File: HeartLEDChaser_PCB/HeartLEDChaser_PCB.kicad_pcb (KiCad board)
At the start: 2 copper layers, 55.6 x 49.3 mm, 34 parts, among them U1 ICM7555CBAZ, U2 CD4017BM, U3 HT7733A, U4 HX SS12F44G4

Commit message: Routed PCB
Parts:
- H1: footprint MountingHole:MountingHole_2.7mm -> MountingHole:MountingHole_2.1mm
- moved C4 84.3 mm to (162.3, 90.4), turned to -90 degrees
- moved U3 83.7 mm to (160.3, 85.8), turned to 90 degrees
- moved S1 79.0 mm to (158.4, 90.4), turned to -90 degrees
- moved D10 77.3 mm to (154.2, 79.4)
- moved D6 77.3 mm to (143.9, 119.8)
- moved D7 77.3 mm to (158.7, 109.8)
- moved D8 77.3 mm to (168.3, 96.3)
- moved R12 77.3 mm to (157.5, 79.4)
- moved R7 77.3 mm to (134.6, 113.6)
- moved R8 77.3 mm to (145.2, 115.4)
- moved R9 77.3 mm to (155.6, 113.5)
- moved D2 77.3 mm to (135.8, 79.3)
- moved D3 77.3 mm to (122.8, 81.4)
- moved D4 77.3 mm to (121.8, 96.3)
- moved D5 77.3 mm to (131.5, 109.8)
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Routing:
- net Net-(D9-A): track 0.00 -> 52.9 mm, vias 0 -> 1
- net +3V3: track 0.00 -> 43.6 mm
- net Net-(D8-A): track 0.00 -> 35.1 mm, vias 0 -> 1
- net Net-(U1-THRESHOLD): track 0.00 -> 31.3 mm
- net Net-(D10-A): track 0.00 -> 30.8 mm, vias 0 -> 1
- net Net-(D3-A): track 0.00 -> 29.3 mm
- net Net-(D6-A): track 0.00 -> 27.5 mm, vias 0 -> 1
- net Net-(D7-A): track 0.00 -> 25.8 mm, vias 0 -> 1
- net Net-(D2-A): track 0.00 -> 24.1 mm, vias 0 -> 1
- net +3V0: track 0.00 -> 23.7 mm
- net ASTABLE_OUTPUT: track 0.00 -> 20.9 mm
- net Net-(D4-A): track 0.00 -> 19.7 mm
- net Net-(D1-A): track 0.00 -> 17.1 mm
- net Net-(D5-A): track 0.00 -> 15.4 mm
- net GND: track 0.00 -> 15.4 mm, vias 0 -> 2
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- added copper zone on B.Cu, net GND
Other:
- board size 55.6 x 49.3 mm -> 55.6 x 49.4 mm

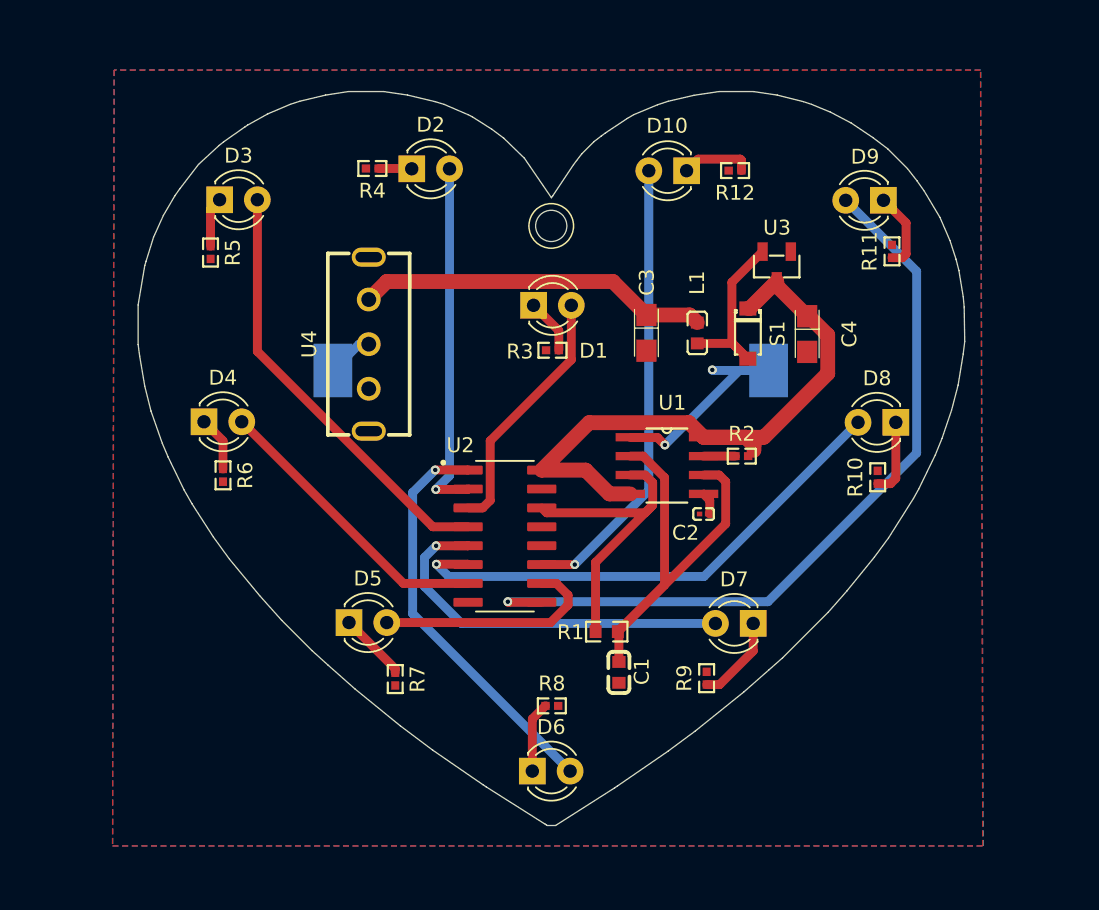
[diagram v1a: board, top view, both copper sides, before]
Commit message: Added logos
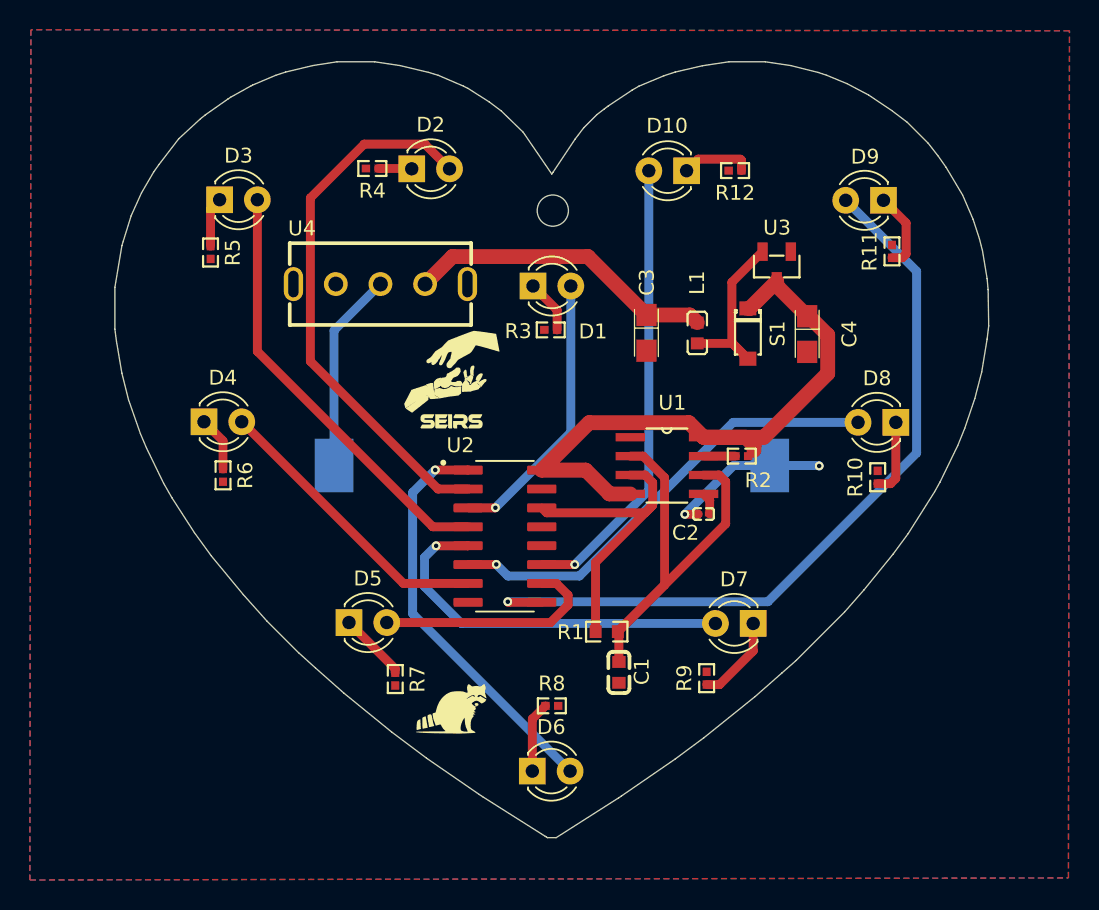
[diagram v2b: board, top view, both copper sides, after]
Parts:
- added G***: LOGO, FOOTPRINTS:seirslogo, F.Cu at (138.4, 93.4)
- added G***: LOGO, FOOTPRINTS:raccoonimage, F.Cu at (138.3, 115.6)
- moved BT1 6.39 mm to (145.2, 99.2)
- moved U4 4.12 mm to (133.7, 87.0), turned to 0 degrees
- moved R3 1.37 mm to (145.1, 90.1)
- moved D1 1.30 mm to (143.9, 87.2)
- moved H1 1.04 mm to (145.2, 82.1)
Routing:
- net Net-(D2-A): track 24.1 -> 36.7 mm, vias 1 -> 0
- net Net-(BT1-+): track 3.14 -> 13.5 mm
- net Net-(D8-A): track 35.1 -> 30.8 mm
- net GND: track 15.4 -> 11.3 mm
- net +3V0: track 23.7 -> 20.9 mm
- net Net-(D1-A): track 17.1 -> 18.8 mm, vias 0 -> 1
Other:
- board size 55.6 x 49.4 mm -> 58.8 x 52.2 mm
- board text added: "Happy Valentine's Day ( ˘ ³˘)♥"
- board text added: "https://github.com/fectec/HeartLEDChaser"

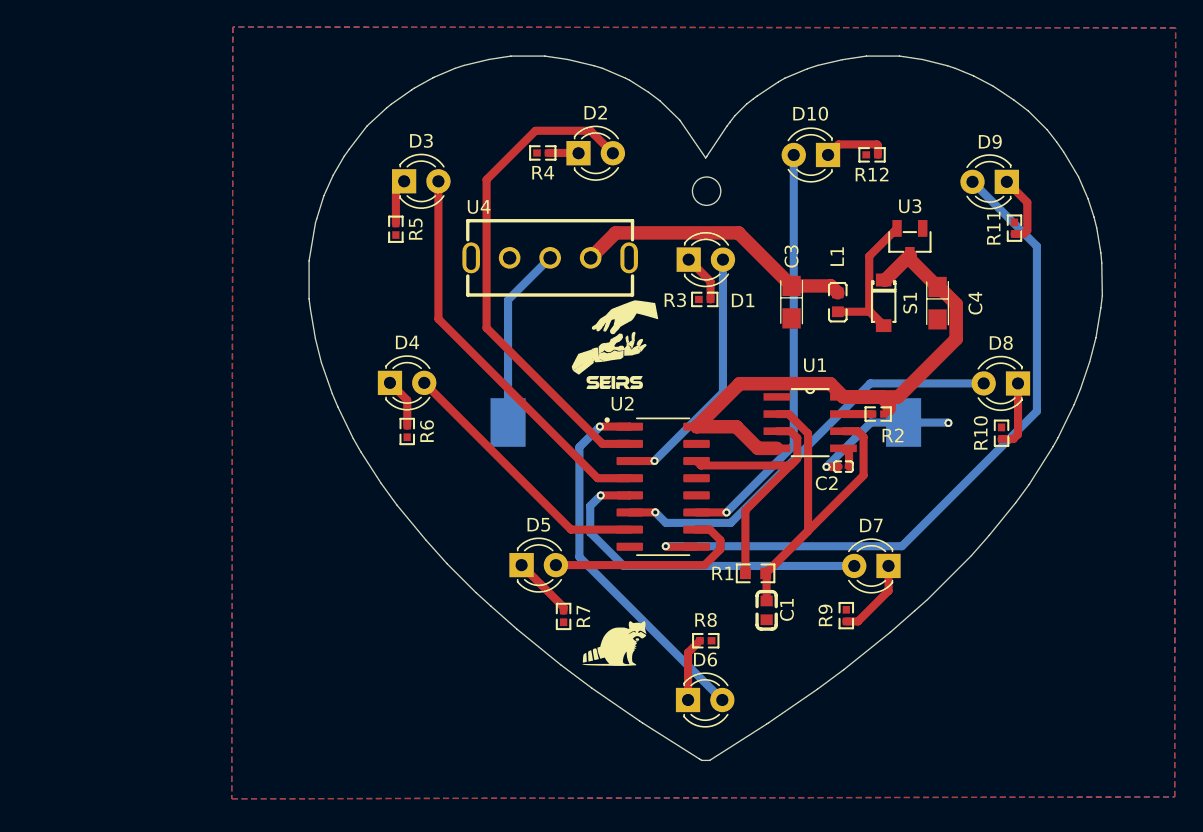
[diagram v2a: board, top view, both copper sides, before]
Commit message: Improved layout & routing
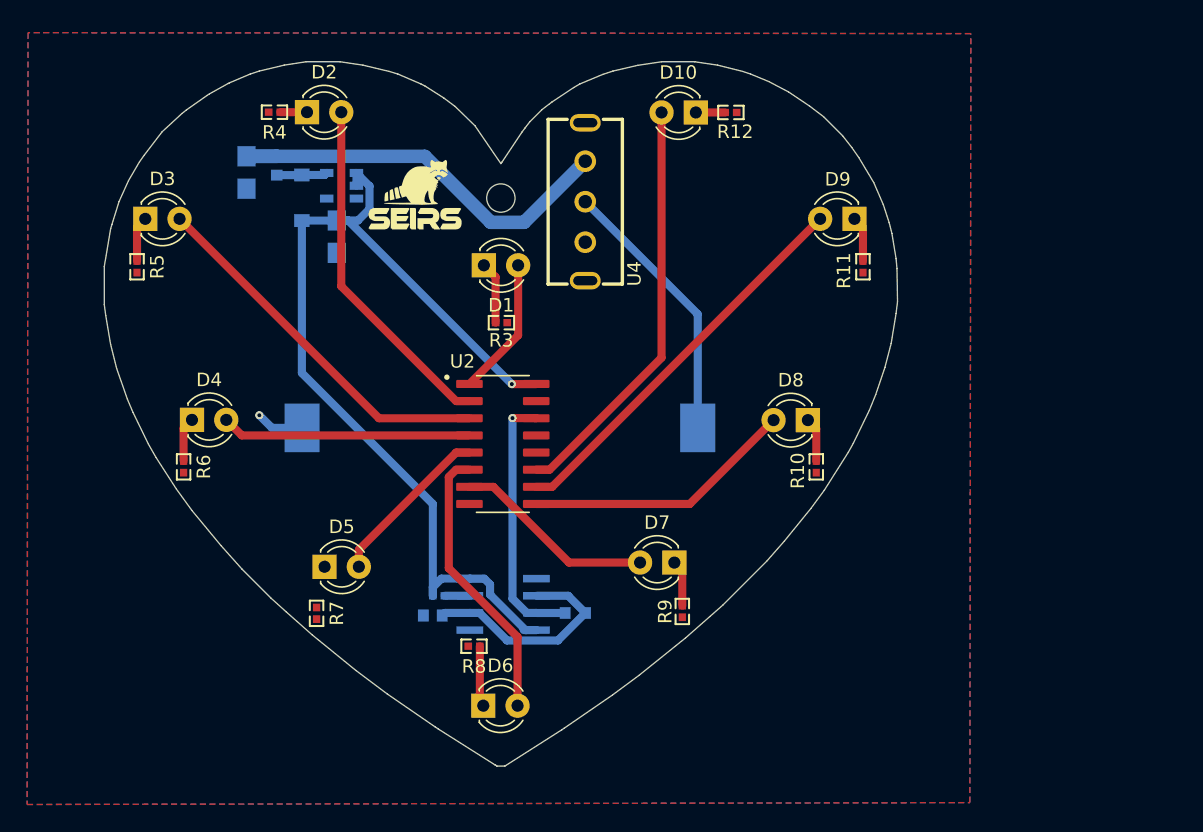
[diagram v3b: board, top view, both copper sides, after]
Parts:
- removed C2: 47nF, FOOTPRINTS:C85925
- C1, C3, C4, L1, R1, R2, S1, U1: moved to B.Cu
- U3: value HT7733A -> HT7750A; footprint FOOTPRINTS:HT7733A -> FOOTPRINTS:HT7750A; moved to B.Cu
- moved C4 44.8 mm to (117.8, 85.5)
- moved S1 43.8 mm to (115.3, 82.6), turned to 90 degrees
- moved L1 42.8 mm to (113.4, 80.2)
- moved U3 42.3 mm to (118.2, 81.7), turned to -90 degrees
- moved C3 41.5 mm to (111.2, 80.7)
- moved G*** 37.2 mm to (123.6, 81.5)
- moved R2 35.2 mm to (125.4, 112.1), turned to 180 degrees
- moved U1 26.4 mm to (130.2, 112.7), turned to 180 degrees
- moved C1 24.7 mm to (125.0, 113.5), turned to 180 degrees
- moved D2 20.3 mm to (115.6, 76.2)
- moved R4 20.1 mm to (113.2, 76.2)
- moved D3 19.4 mm to (103.7, 84.1)
- moved R5 19.4 mm to (103.0, 87.7)
- moved R7 18.3 mm to (116.3, 113.4)
- moved G*** 17.4 mm to (123.6, 84.2)
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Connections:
- C4 pad 1: +3V3 -> +5V
- D5 pad 1: Net-(D5-K) -> unconnected-(D5-K-Pad1)
- R2 pad 2: +3V3 -> +5V
- R7 pad 1: Net-(D5-K) -> unconnected-(R7-Pad1)
- R7 pad 2: GND -> unconnected-(R7-Pad2)
- S1 pad 1: +3V3 -> +5V
- U1 pad 4: +3V3 -> +5V
- U1 pad 5: Net-(U1-CONTROL_VOLTAGE) -> GND
- U1 pad 8: +3V3 -> +5V
- U2 pad 1: Net-(D6-A) -> Net-(D1-A)
- U2 pad 10: Net-(D5-A) -> Net-(D9-A)
- U2 pad 16: +3V3 -> +5V
- U2 pad 3: Net-(D1-A) -> Net-(D3-A)
- U2 pad 4: Net-(D3-A) -> Net-(D4-A)
- U2 pad 5: Net-(D7-A) -> Net-(D5-A)
- U2 pad 6: Net-(D8-A) -> Net-(D6-A)
- U2 pad 7: Net-(D4-A) -> Net-(D7-A)
- U2 pad 9: Net-(D9-A) -> Net-(D8-A)
- U3 pad 1: GND -> +5V
- U3 pad 2: Net-(S1-A) -> +5V
- U3 pad 3: +3V3 -> unconnected-(U3-NC-Pad3)
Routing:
- net +5V: track 0.00 -> 72.5 mm, vias 0 -> 1
- net +3V3: track 43.6 -> 0.00 mm
- net Net-(D9-A): track 52.9 -> 29.3 mm, vias 1 -> 0
- net Net-(U1-THRESHOLD): track 31.3 -> 16.5 mm
- net Net-(D7-A): track 25.8 -> 15.0 mm, vias 1 -> 0
- net Net-(D2-A): track 36.7 -> 25.9 mm
- net Net-(D8-A): track 30.8 -> 20.2 mm, vias 1 -> 0
- net +3V0: track 20.9 -> 31.2 mm
- net Net-(S1-A): track 12.3 -> 3.75 mm
- net Net-(D1-A): track 18.8 -> 10.3 mm, vias 1 -> 0
- net GND: track 11.3 -> 3.56 mm, vias 2 -> 1
- net Net-(BT1-+): track 13.5 -> 20.2 mm
- net Net-(D6-A): track 27.5 -> 20.8 mm, vias 1 -> 0
- net Net-(D5-K): track 4.66 -> 0.00 mm
- net Net-(D7-K): track 5.92 -> 2.60 mm
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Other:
- board text added: "github.com/ fectec/ HeartLEDChaser"
- board text removed: "https://github.com/fectec/HeartLEDChaser"

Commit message: Cleanup
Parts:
- moved G*** 0.36 mm to (123.5, 84.5)
- moved G*** 0.29 mm to (123.5, 81.7)
- turned R7 to 90 degrees
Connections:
- D5 pad 1: unconnected-(D5-K-Pad1) -> Net-(D5-K)
- R7 pad 1: unconnected-(R7-Pad1) -> GND
- R7 pad 2: unconnected-(R7-Pad2) -> Net-(D5-K)
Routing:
- net Net-(D5-K): track 0.00 -> 3.26 mm
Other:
- board text added: "© 2025"
